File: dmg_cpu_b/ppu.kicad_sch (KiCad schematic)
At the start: 0 parts

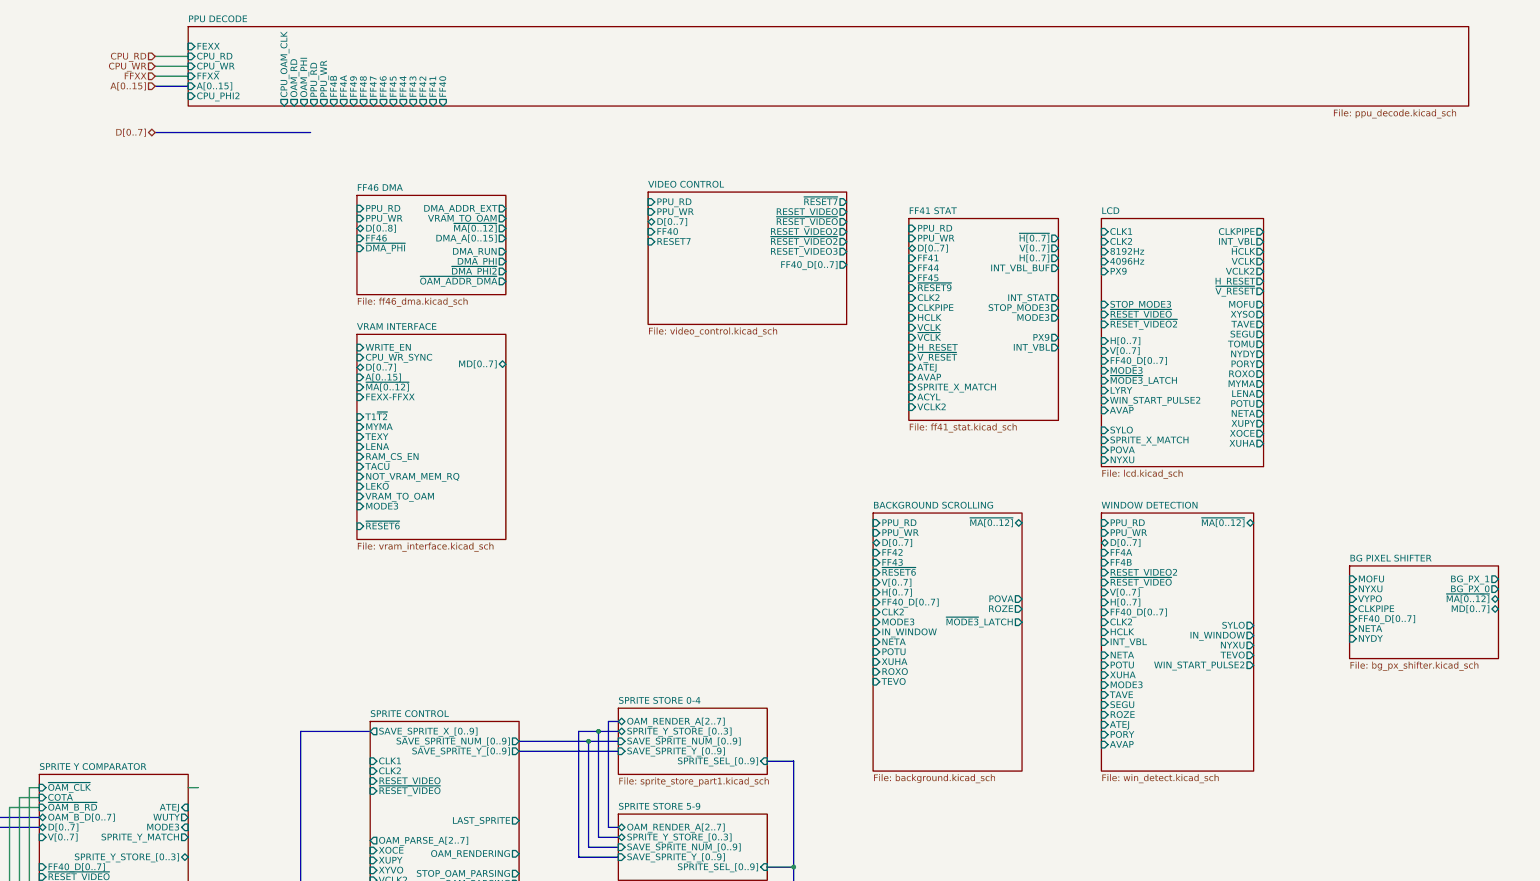
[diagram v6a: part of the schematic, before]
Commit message: All sheets captured. Serious tidying is required in PPU section.
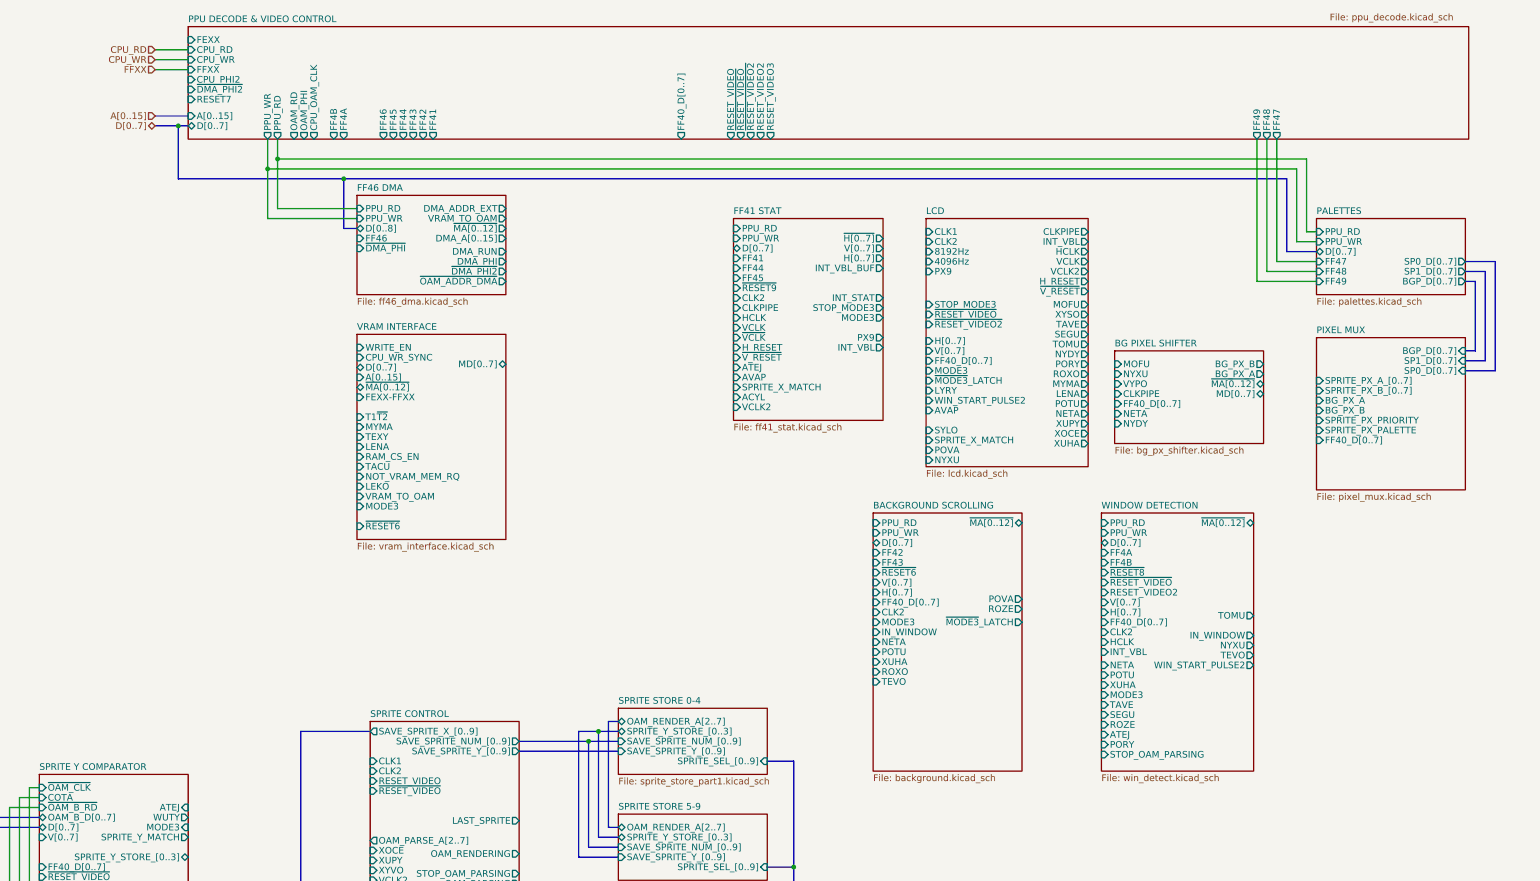
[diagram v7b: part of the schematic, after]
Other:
- sheet PPU DECODE renamed PPU DECODE & VIDEO CONTROL
- sheet VIDEO CONTROL renamed PALETTES
- added sheet PIXEL MUX (pixel_mux.kicad_sch)
- sheet BG PIXEL SHIFTER ports: added BG_PX_A, BG_PX_B; removed BG_PX_0, BG_PX_1
- sheet PALETTES: file video_control.kicad_sch -> palettes.kicad_sch
- sheet PALETTES ports: added BGP_D[0..7], FF47, FF48, FF49, SP0_D[0..7], SP1_D[0..7]; removed FF40, FF40_D[0..7], RESET7, RESET_VIDEO, RESET_VIDEO2, RESET_VIDEO3, ~{RESET7}, ~{RESET_VIDEO2}, ~{RESET_VIDEO}
- sheet PPU DECODE & VIDEO CONTROL ports: added D[0..7], FF40_D[0..7], RESET7, RESET_VIDEO, RESET_VIDEO2, RESET_VIDEO3, ~{DMA_PHI2}, ~{RESET_VIDEO2}, ~{RESET_VIDEO}; removed FF40
- sheet WINDOW DETECTION ports: added STOP_OAM_PARSING, TOMU, ~{RESET8}; removed AVAP, SYLO

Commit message: New sheet created to free up space on LCD and SCX/SCY sheets and joined common signals.
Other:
- added sheet BG & WIN CYCLES (bg_win_cycles.kicad_sch)
- sheet BACKGROUND SCROLLING ports: added BP_CY, BP_SEL, TM_CY; removed CLK2, MODE3, NETA, POTU, POVA, ROXO, ROZE, TEVO, XUHA, ~{MODE3}_LATCH
- sheet BG PIXEL SHIFTER ports: added BP_CY; removed NETA, VYPO
- sheet FF41 STAT ports: added MODE1, STOP_OAM_PARSING; removed ACYL, AVAP, ~{VCLK}
- sheet LCD ports: added none; removed AVAP, CLK2, CLKPIPE, H[0..7], H_RESET, LENA, LYRY, MODE3, MOFU, MYMA, NETA, NYDY, NYXU, PORY, POTU, POVA, PX9, ROXO, SEGU, SPRITE_X_MATCH, STOP_MODE3, SYLO, TAVE, TOMU, WIN_START_PULSE2, XUHA, ~{MODE3}_LATCH
- sheet VRAM INTERFACE ports: added TM_BP_CYS, ~{TM_BP_CYS}; removed LENA, MYMA
- sheet WINDOW DETECTION ports: added BP_CY, BP_SEL, TM_CY; removed NETA, POTU, XUHA
